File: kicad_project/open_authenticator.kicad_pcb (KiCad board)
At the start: 2 copper layers, 82 x 42 mm, 54 parts, among them IC1 TPS22919DCKR, J1 Conn_01x02_Female, J2 TYPE-C-31-M-17, J3 Conn_01x02_Female, Q1 DMP2305U-7, SW1 UP, SW2 DOWN, SW3 BOOT/SELECT, SW4 RESET, SW5 POWER SWITCH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

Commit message: Added gerber files
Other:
- rule pad_to_mask_clearance: 0.000051 -> 0
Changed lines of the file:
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@@
     (pad_size 2.2 3.5)
     (pad_drill 1.5)
-    (pad_to_mask_clearance 0.000051)
+    (pad_to_mask_clearance 0)
     (aux_axis_origin 0 0)
     (visible_elements 7FFFFFFF)
@@
       (drillshape 0)
       (scaleselection 1)
-      (outputdirectory "gerber/"))
+      (outputdirectory "../gerber/"))
   )
   (net 0 "")

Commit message: Updated PCB and gerber, also added datasheet of battery
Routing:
- net GND: track 291.4 -> 288.9 mm, vias 112 -> 110
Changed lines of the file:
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@@
     (thickness 1.6)
     (drawings 31)
-    (tracks 715)
+    (tracks 711)
     (zones 0)
     (modules 54)
@@
     (tags "Integrated Circuit")
     (attr smd)
-    (fp_text reference IC1 (at -2.55 -0.05 180) (layer F.SilkS)
+    (fp_text reference IC1 (at -2.5434 0.458 180) (layer F.SilkS)
       (effects (font (size 1 1) (thickness 0.2)))
     )
@@
     (effects (font (size 0.75 0.75) (thickness 0.1875)))
   )
-  (gr_circle (center 131.9 85.45) (end 131.9 85.25) (layer F.SilkS) (width 0.15))
+  (gr_circle (center 134.3914 84.963) (end 134.3914 84.763) (layer F.SilkS) (width 0.15))
   (gr_circle (center 133.25 101.9) (end 133.532843 101.9) (layer F.SilkS) (width 0.15))
   (gr_circle (center 103.15 111.75) (end 103.720088 111.75) (layer F.SilkS) (width 0.15))
@@
   (via (at 162.306 81.153) (size 0.8) (drill 0.4) (layers F.Cu B.Cu) (net 3))
   (via (at 159.893 81.153) (size 0.8) (drill 0.4) (layers F.Cu B.Cu) (net 3))
-  (via (at 161.4932 84.963) (size 0.8) (drill 0.4) (layers F.Cu B.Cu) (net 3))
-  (segment (start 161.4932 84.963) (end 160.9852 85.471) (width 0.5) (layer F.Cu) (net 3))
-  (via (at 160.9852 87.249) (size 0.8) (drill 0.4) (layers F.Cu B.Cu) (net 3))
-  (segment (start 160.9852 85.471) (end 160.9852 87.249) (width 0.5) (layer F.Cu) (net 3))
   (segment (start 96.5 113.18) (end 98.465 111.215) (width 0.5) (layer F.Cu) (net 3))
   (segment (start 96.5 113.2) (end 96.5 113.18) (width 0.5) (layer F.Cu) (net 3))

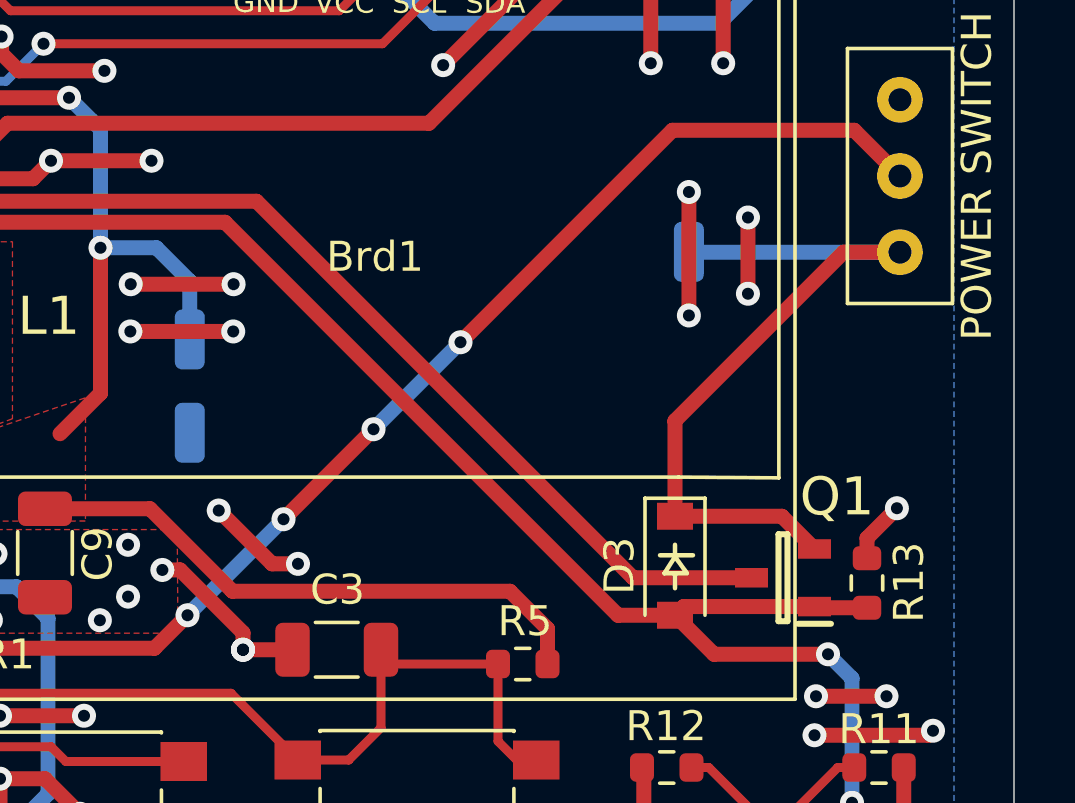
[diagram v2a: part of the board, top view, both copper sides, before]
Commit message: Updated placement of certain components and pads
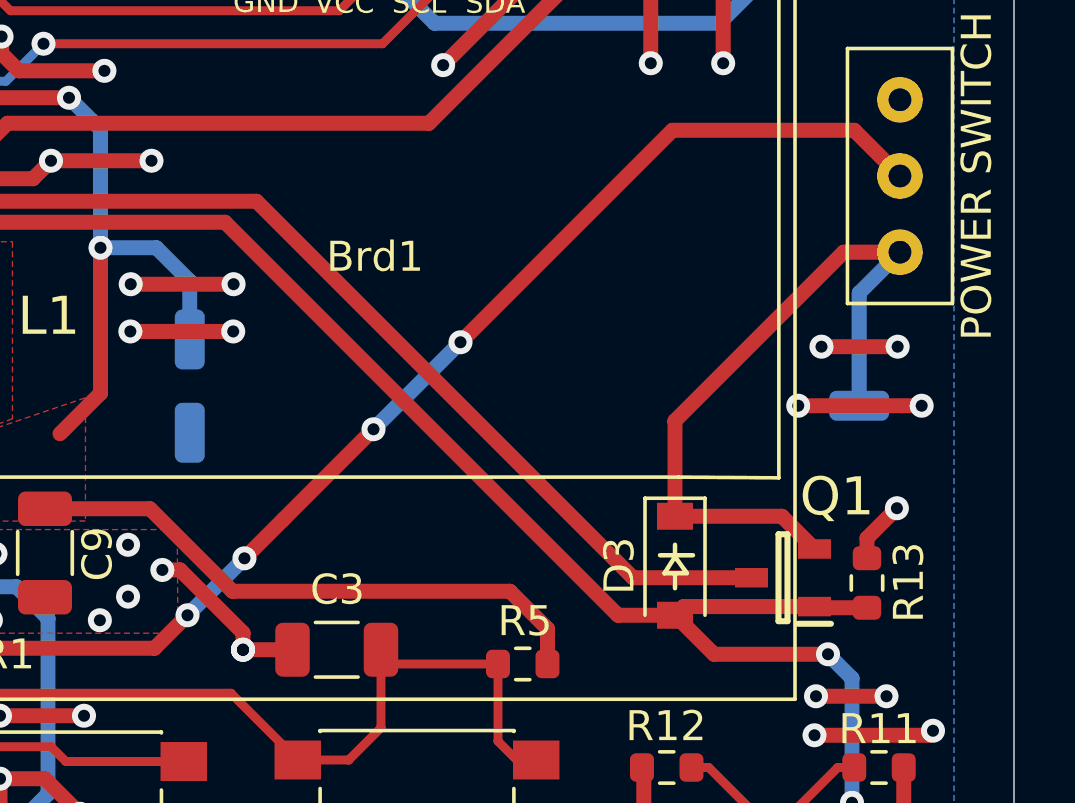
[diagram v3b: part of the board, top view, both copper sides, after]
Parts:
- moved TP5 7.65 mm to (166.8, 98.7), turned to 90 degrees
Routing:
- net GND: track 288.9 -> 285.5 mm, vias 110 -> 108
- net /V_INPUT: track 25.2 -> 23.8 mm

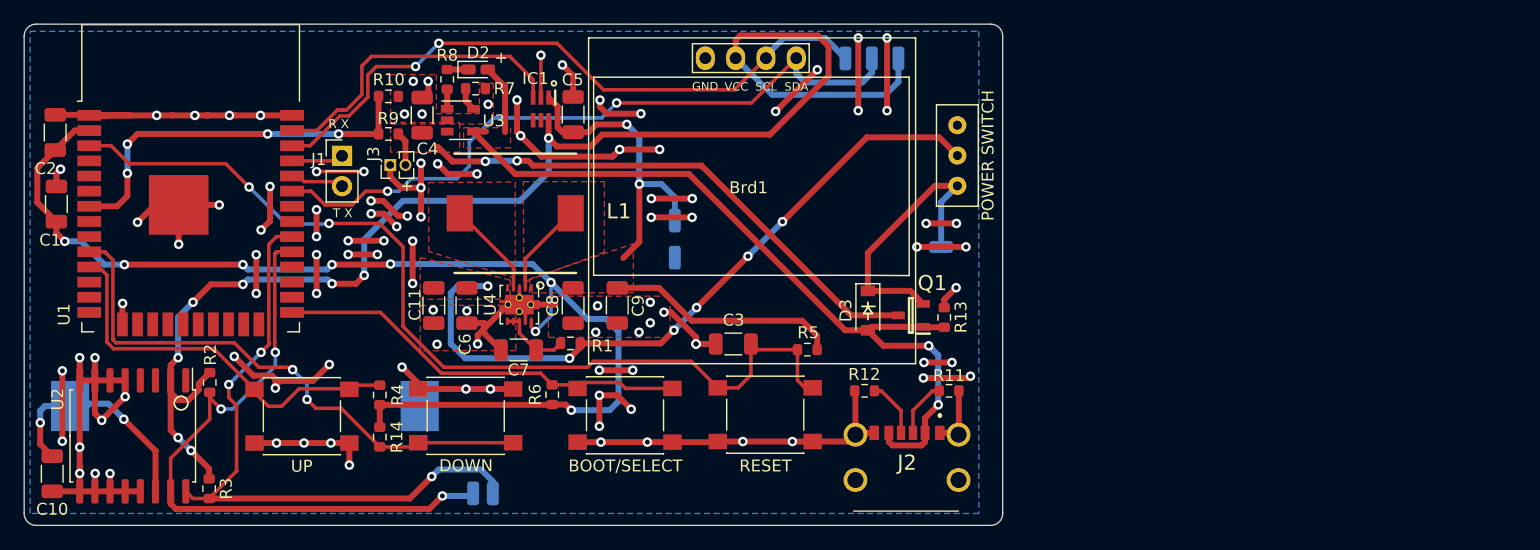
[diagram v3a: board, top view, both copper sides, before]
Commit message: Added 3D-models of majority components and added schematics of bare oled-panel, assigned footprints, routing is to be done
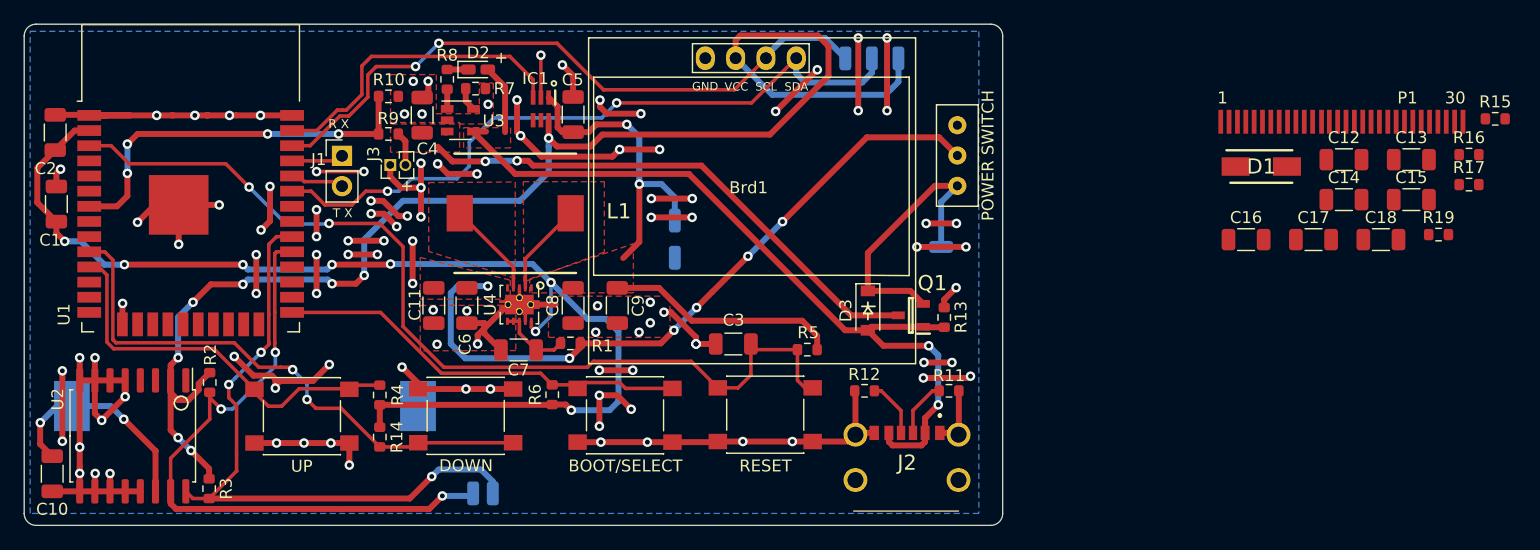
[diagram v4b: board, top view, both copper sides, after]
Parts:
- added C12: 10uF 50V, Capacitor_SMD:C_1206_3216Metric, F.Cu at (200.6, 91.4)
- added C13: 0.1uF 50V, Capacitor_SMD:C_1206_3216Metric, F.Cu at (206.2, 91.4)
- added C14: 0.1uF 50V, Capacitor_SMD:C_1206_3216Metric, F.Cu at (200.6, 94.7)
- added C15: 4.7uF 50V, Capacitor_SMD:C_1206_3216Metric, F.Cu at (206.2, 94.7)
- added C16: 2.2uF 50V, Capacitor_SMD:C_1206_3216Metric, F.Cu at (192.4, 98.1)
- added C17: 1uF 16V, Capacitor_SMD:C_1206_3216Metric, F.Cu at (198.0, 98.1)
- added C18: 1uF 16V, Capacitor_SMD:C_1206_3216Metric, F.Cu at (203.7, 98.1)
- added D1: SS14, SS14:DIOM5227X270N, F.Cu at (193.7, 91.9)
- added P1: SSD1306_ribbon, ribbon_connectors:SSD1306_ribbon, F.Cu at (200.4, 88.2)
- added R15: 4.7k, Resistor_SMD:R_0603_1608Metric, F.Cu at (213.3, 87.9)
- added R16: 4.7k, Resistor_SMD:R_0603_1608Metric, F.Cu at (211.1, 90.9)
- added R17: 4.7k, Resistor_SMD:R_0603_1608Metric, F.Cu at (211.1, 93.4)
- added R19: 910k, Resistor_SMD:R_0603_1608Metric, F.Cu at (208.5, 97.6)
- BT1: footprint BU2032SM-BT-GTR:BU2032SMBTGTR -> CR2032-BS-6-1:CR2032BS61
- turned BT1 to 270 degrees
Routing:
- net Net-(BT1-Pad1): track 17.8 -> 18.4 mm
